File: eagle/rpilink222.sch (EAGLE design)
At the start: 61 parts, among them IC1 IMS-C011M2S20E, IC2 MCP23017SO, IC3 SM77H, IC4 '244, IC5 MAX3467EPA, IC6 MAX3467EPA, IC7 MAX3467EPA, X1 RASPI_BOARD_AB_E2P

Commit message: Added CERN_OHR license information.
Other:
- note added: "Copyright (C) 2014 Hessel Schut"
- note added: "RPi Link Adaptor"
- note added: "This project is licensed under the CERN Open Hardware Licence v1.2."
- note added: "v.2.22"
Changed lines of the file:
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@@
 </layers>
 <schematic xreflabel="%F%N/%S.%C%R" xrefpart="/%S.%C%R">
+<description>Raspberry Pi Link Adaptor v2.22,
+Copyright (C) 2014 Hessel Schut</description>
 <attributes>
 </attributes>
@@
 <text x="7.62" y="12.7" size="1.778" layer="91">i2c address
 selection</text>
+<wire x1="269.24" y1="157.48" x2="297.18" y2="157.48" width="0.1524" layer="95"/>
+<wire x1="297.18" y1="157.48" x2="335.28" y2="157.48" width="0.1524" layer="95"/>
+<wire x1="335.28" y1="157.48" x2="335.28" y2="149.86" width="0.1524" layer="95"/>
+<wire x1="335.28" y1="149.86" x2="335.28" y2="144.78" width="0.1524" layer="95"/>
+<wire x1="335.28" y1="144.78" x2="335.28" y2="134.62" width="0.1524" layer="95"/>
+<wire x1="335.28" y1="134.62" x2="269.24" y2="134.62" width="0.1524" layer="95"/>
+<wire x1="269.24" y1="134.62" x2="269.24" y2="144.78" width="0.1524" layer="95"/>
+<text x="271.78" y="152.4" size="1.778" layer="95">RPi Link Adaptor</text>
+<text x="299.72" y="152.4" size="1.778" layer="95">v.2.22</text>
+<wire x1="269.24" y1="144.78" x2="269.24" y2="149.86" width="0.1524" layer="95"/>
+<wire x1="269.24" y1="149.86" x2="269.24" y2="157.48" width="0.1524" layer="95"/>
+<wire x1="269.24" y1="149.86" x2="297.18" y2="149.86" width="0.1524" layer="95"/>
+<text x="271.78" y="147.32" size="1.778" layer="95">Copyright (C) 2014 Hessel Schut</text>
+<wire x1="297.18" y1="149.86" x2="335.28" y2="149.86" width="0.1524" layer="95"/>
+<wire x1="269.24" y1="144.78" x2="335.28" y2="144.78" width="0.1524" layer="95"/>
+<wire x1="297.18" y1="152.4" x2="297.18" y2="157.48" width="0.1524" layer="95"/>
+<wire x1="297.18" y1="157.48" x2="297.18" y2="149.86" width="0.1524" layer="95"/>
+<text x="271.78" y="137.16" size="1.778" layer="95">This project is licensed under the
+CERN Open Hardware Licence v1.2.</text>
 </plain>
 <instances>

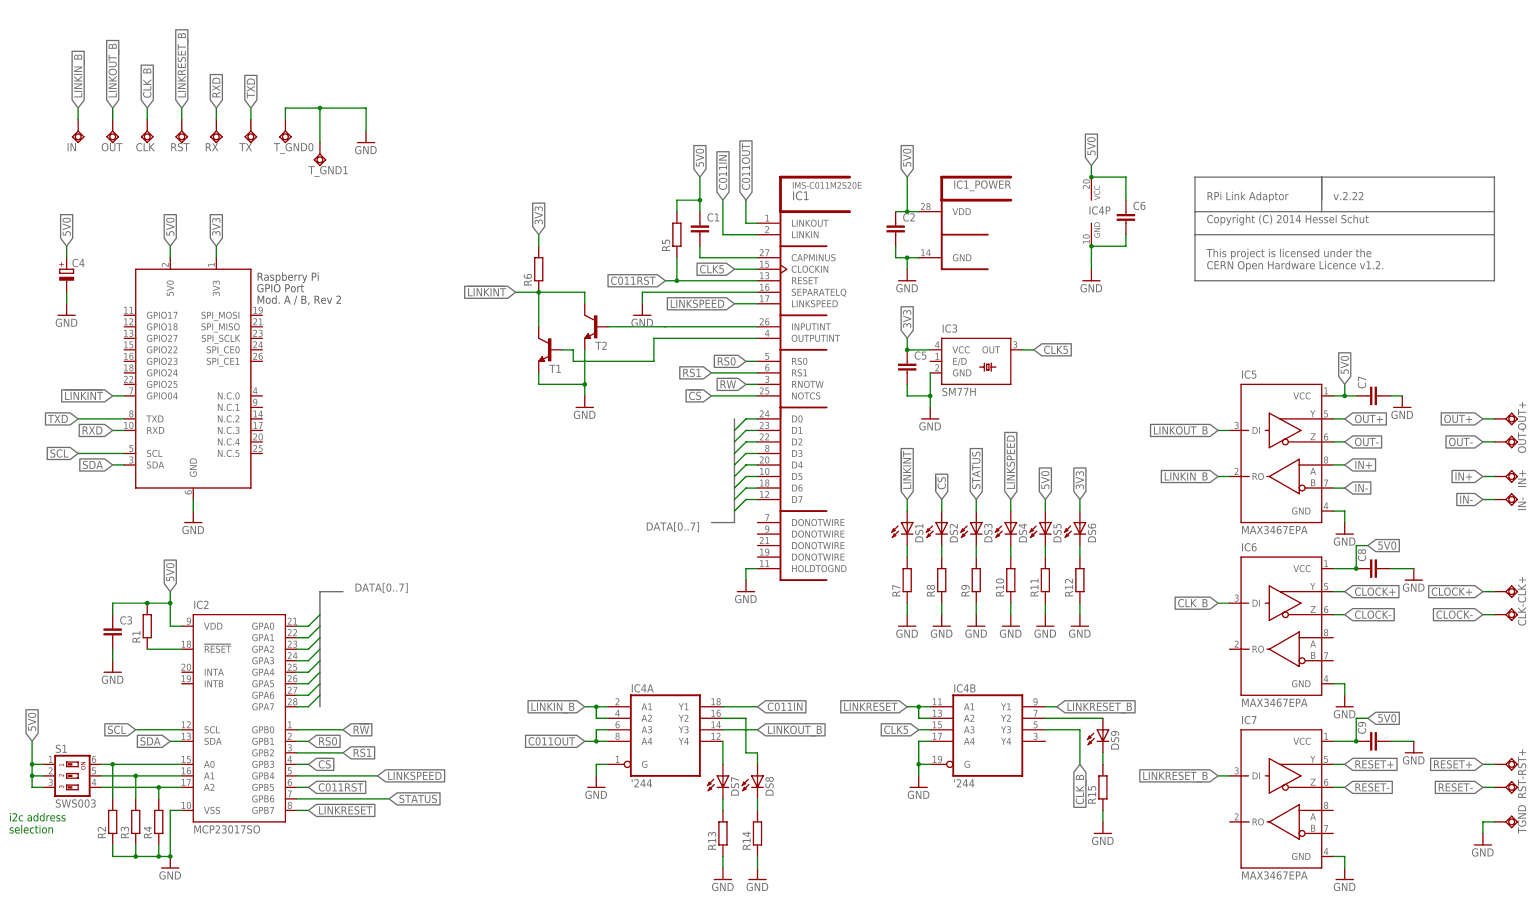
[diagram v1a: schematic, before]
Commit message: Added component values, added rs-422 bias resistors.
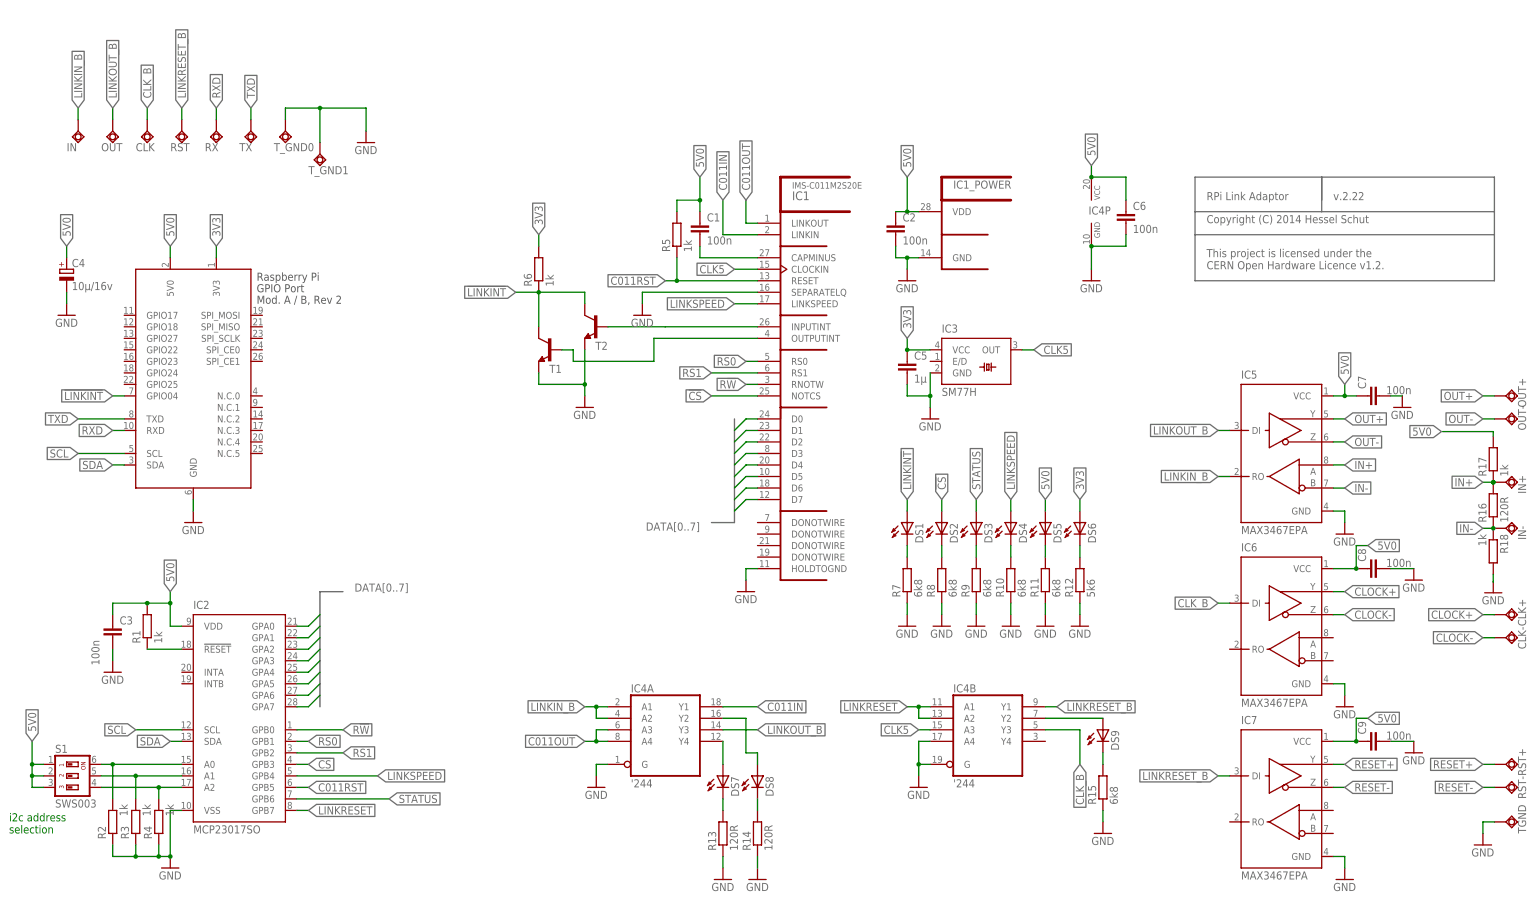
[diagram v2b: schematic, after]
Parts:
- added R16: 120R, rcl:R-EU_R0603
- added R17, R18: 1k, rcl:R-EU_R0603
- C1, C2, C3, C6, C7, C8, C9: value (none) -> 100n
- C4: value (none) -> 10µ/16v
- C5: value (none) -> 1µ
- R1, R2, R3, R4, R5, R6: value (none) -> 1k
- R10, R11, R15, R7, R8, R9: value (none) -> 6k8
- R12: value (none) -> 5k6
- R13, R14: value (none) -> 120R
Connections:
- net 5V0: now also R17.2
- net GND: now also R18.2
- net IN+: now also R16.2, R17.1
- net IN-: now also R16.1, R18.1
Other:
- moved on the sheet: CLK+, CLK-, IN+, IN-, OUT+, OUT-
